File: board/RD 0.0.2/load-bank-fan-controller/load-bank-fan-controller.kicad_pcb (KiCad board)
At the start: 2 copper layers, 66.3 x 54.8 mm, 45 parts, among them J1 FAN1, J2 FAN2, J3 FAN3, J4 SPI, J5 UART, J6 12V IN, J7 TEMP1, J8 TEMP2, J9 RELAY, Q1 IRLML0030, Q2 IRLML0030, SW1 RESET, U1 AMS1117-5.0, U2 ATmega328P-A, U3 LM2904, Y1 Crystal

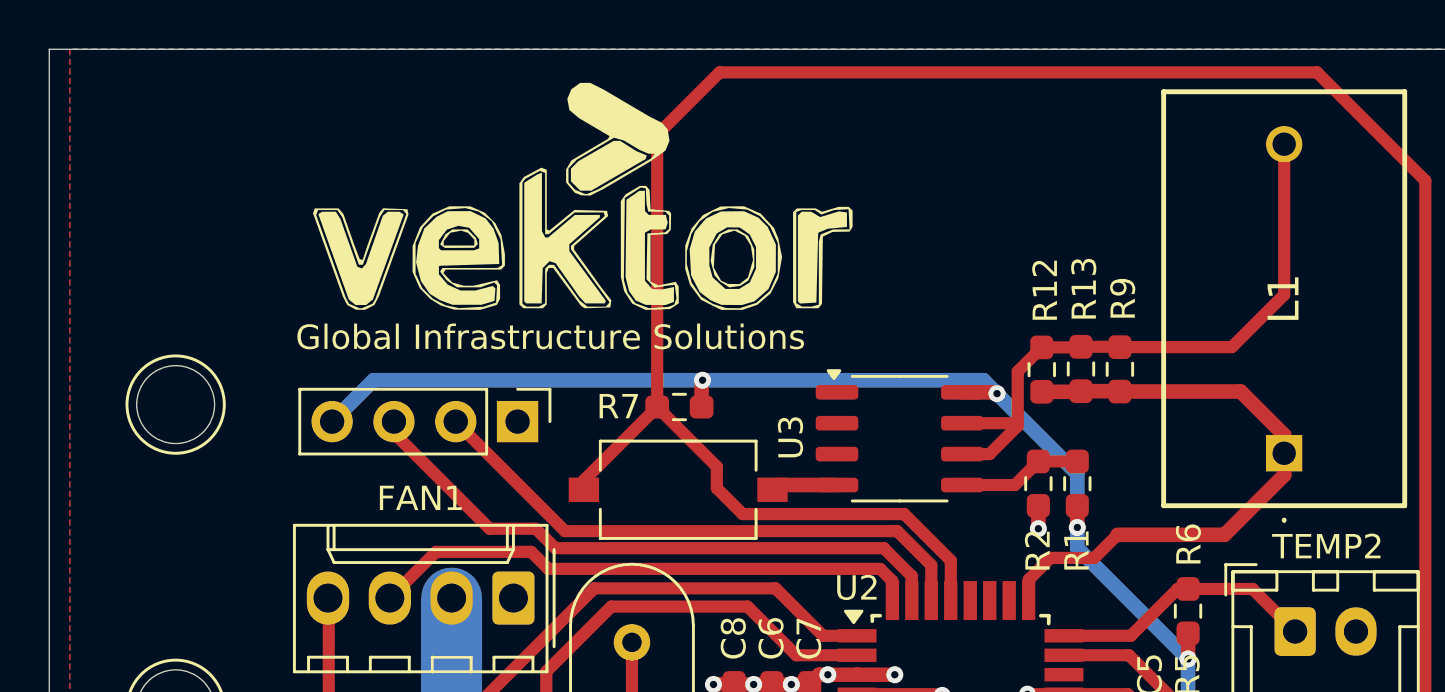
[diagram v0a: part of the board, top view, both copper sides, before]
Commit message: replace current sense resistor with the proper one
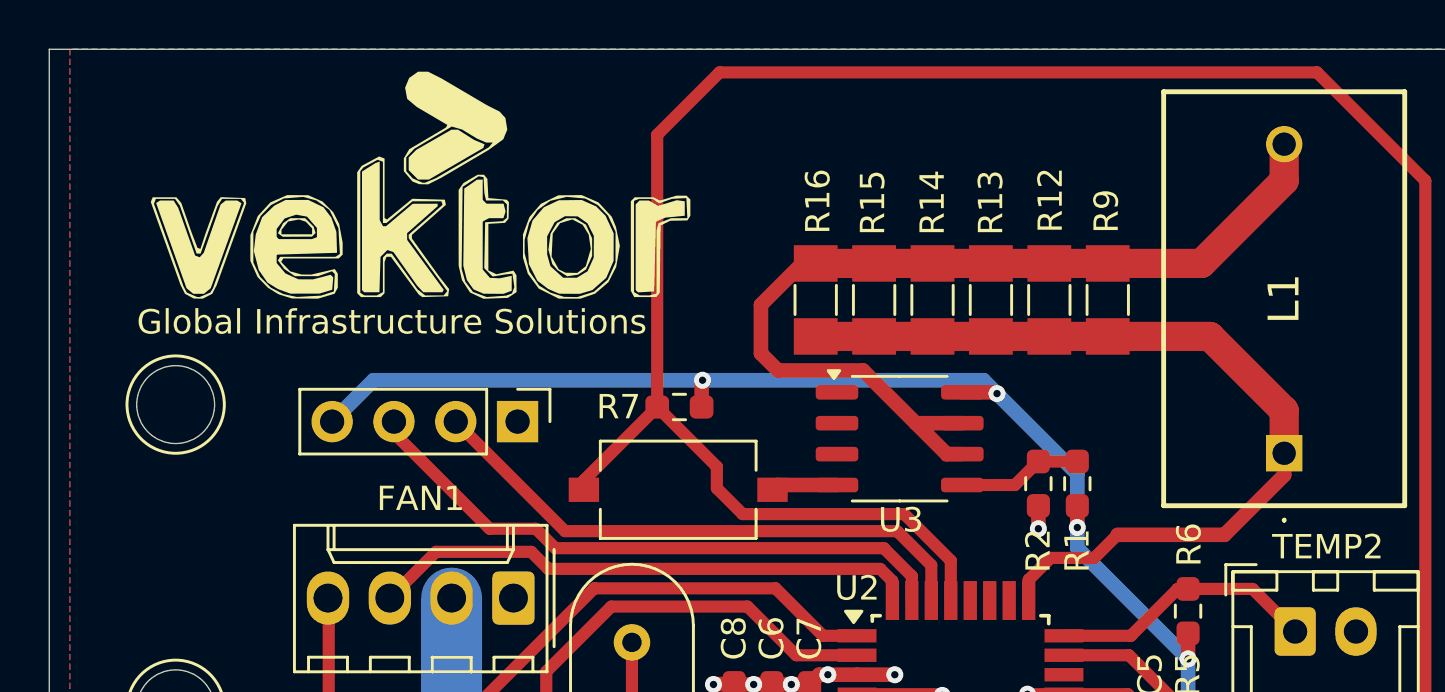
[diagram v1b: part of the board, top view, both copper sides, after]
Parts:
- added R14: 50R, Resistor_SMD:R_MiniMELF_MMA-0204, F.Cu at (145.3, 85.7)
- added R15: 50R, Resistor_SMD:R_MiniMELF_MMA-0204, F.Cu at (142.9, 85.7)
- added R16: 50R, Resistor_SMD:R_MiniMELF_MMA-0204, F.Cu at (140.6, 85.7)
- R12, R13, R9: value 25R -> 50R; footprint Resistor_SMD:R_0603_1608Metric_Pad0.98x0.95mm_HandSolder -> Resistor_SMD:R_MiniMELF_MMA-0204
- moved R13 4.66 mm to (147.8, 85.7)
- moved R9 2.89 mm to (152.6, 85.7)
- moved R12 2.88 mm to (150.2, 85.7)
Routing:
- net Net-(U3B--): track 25.8 -> 39.0 mm
- net CT: track 25.5 -> 36.3 mm

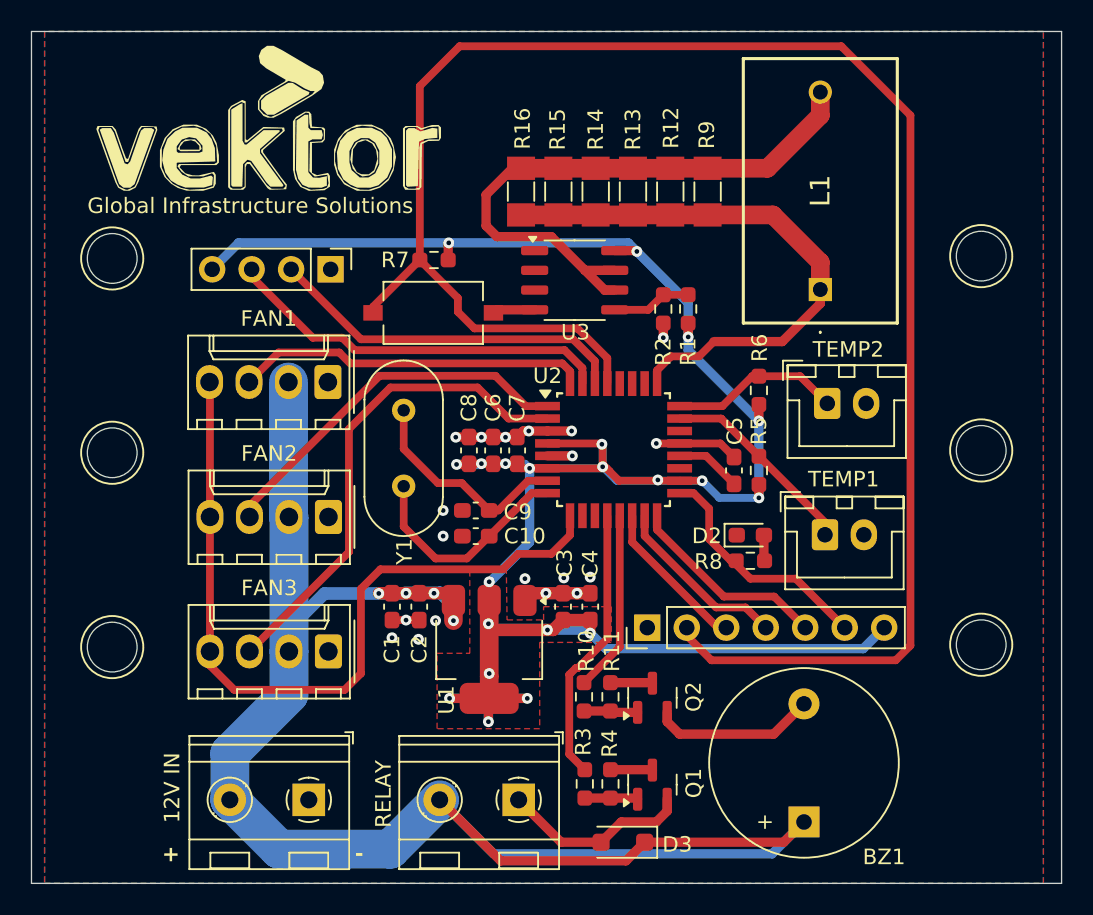
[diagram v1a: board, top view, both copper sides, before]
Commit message: connector changed and component added
change 12v connector, change spi to icsp connector, change  regulator input cap to 100u, remove uart conn, add diode to regulator input
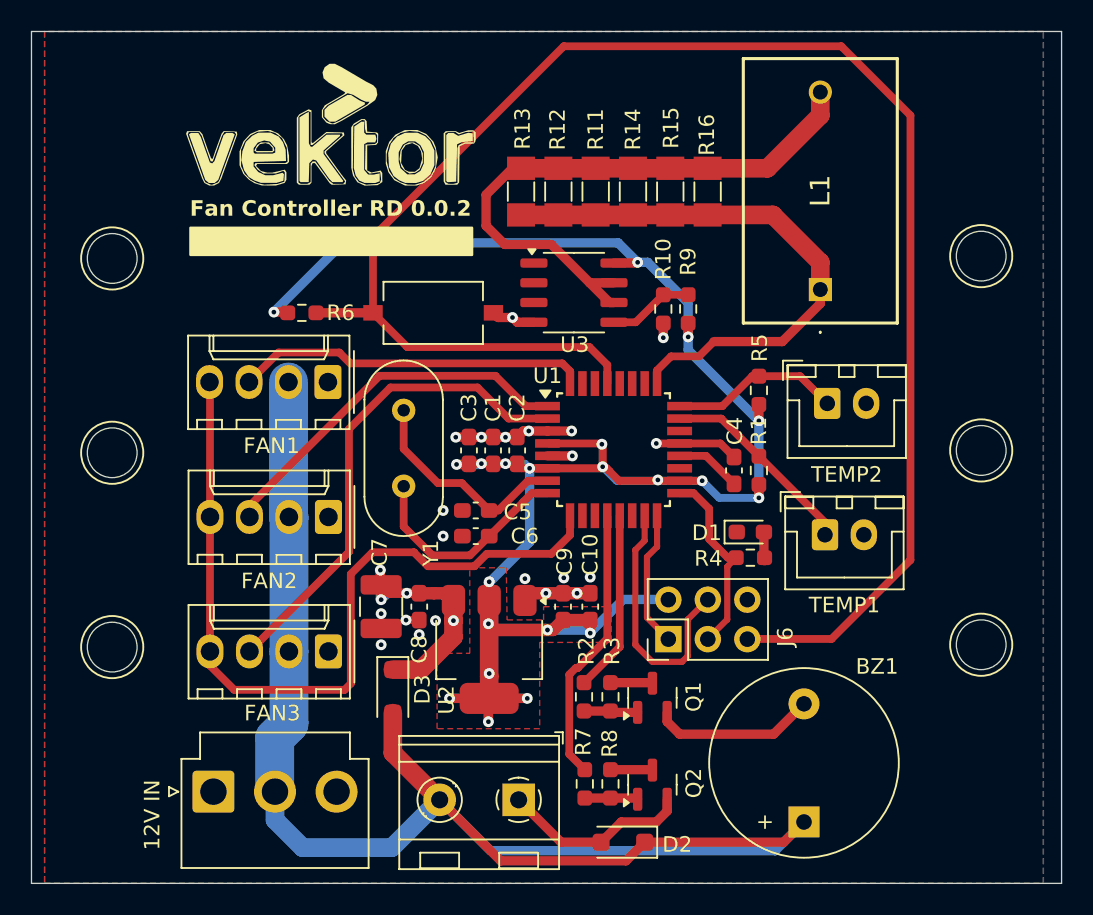
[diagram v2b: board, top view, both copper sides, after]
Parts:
- removed the J4 at (148.7, 113.7)
- removed the J5 at (128.3, 90.7)
- added D3: 1N4007, Diode_SMD:D_SOD-123F, F.Cu at (132.3, 117.8)
- added J8: 12V IN, Connector_JST:JST_VH_B3P-VH-B_1x03_P3.96mm_Vertical, F.Cu at (120.8, 124.2)
- C7: renamed from C1; value 1uF -> 100uF; footprint Capacitor_SMD:C_0603_1608Metric_Pad1.08x0.95mm_HandSolder -> Inductor_SMD:L_1210_3225Metric
- J6: value 12V IN -> ISP; footprint TerminalBlock_RND:TerminalBlock_RND_205-00232_1x02_P5.08mm_Horizontal -> Connector_PinHeader_2.54mm:PinHeader_2x03_P2.54mm_Vertical
- moved J6 25.3 mm to (150.0, 114.4), turned to 90 degrees
- moved R6 9.15 mm to (126.5, 93.5), turned to 0 degrees
- moved U3 0.80 mm to (143.9, 92.2)
- moved C7 0.70 mm to (131.6, 112.3)
- moved D1 0.20 mm to (155.3, 107.5)
- moved R4 0.20 mm to (155.3, 109.2)
- renumbered C6 to C1, C4 to C10, C7 to C2, C8 to C3, C5 to C4, C9 to C5, C10 to C6, C2 to C8, C3 to C9, D2 to D1, D3 to D2, DRA2 to DRA1, DRA1 to DRA2, J7 to J2, J9 to J3, J8 to J4, J2 to J5, J3 to J7, Q2 to Q1, Q1 to Q2, R5 to R1, R2 to R10, R14 to R11, R15 to R12, R16 to R13, R13 to R14, R12 to R15, R9 to R16, R10 to R2, R11 to R3, R8 to R4, R6 to R5, R7 to R6, R3 to R7, R4 to R8, R1 to R9, U2 to U1, U1 to U2
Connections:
- C7 pad 1: +12V -> +12VA
- C8 pad 1: +12V -> +12VA
- J6 pad 1: GND -> MISO
- J6 pad 2: +12V -> +5V
- U2 pad 3: +12V -> +12VA
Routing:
- net uC_TX: track 25.2 -> 0.00 mm
- net uC_RX: track 23.4 -> 0.00 mm
- net +12VA: track 0.00 -> 21.5 mm, vias 0 -> 4
- net +12V: track 121.2 -> 101.1 mm, vias 4 -> 0
- net +5V: track 168.7 -> 151.8 mm
- net SS: track 10.0 -> 0.00 mm
- net RESET: track 117.2 -> 108.9 mm
- net MOSI: track 11.5 -> 16.7 mm
- net MISO: track 13.0 -> 8.76 mm
- net SCK: track 15.5 -> 12.5 mm
- net FAN_PWM: track 50.6 -> 52.3 mm
- net GND: track 29.2 -> 28.7 mm, vias 19 -> 21
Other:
- board text removed: "+"
- board text removed: "-"
- board text removed: "Global Infrastructure Solutions"

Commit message: straighten the din rail mount
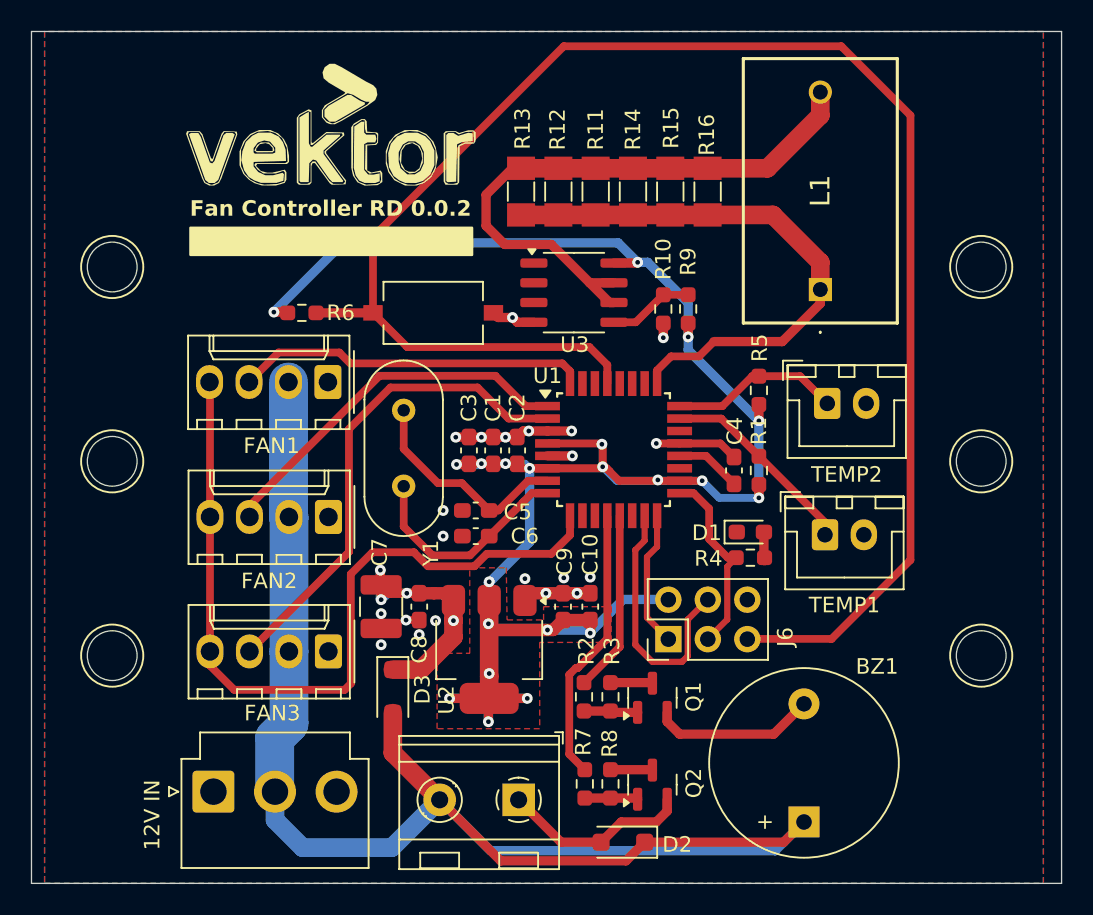
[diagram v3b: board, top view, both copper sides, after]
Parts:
- moved DRA1 0.70 mm to (170.2, 103.0)
- moved DRA2 0.55 mm to (114.2, 103.0)
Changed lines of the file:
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@@
 	(footprint "MountingEquipment:DINRailAdapter_3xM3_PhoenixContact_1201578"
 		(layer "F.Cu")
-		(at 170.15 102.3 90)
+		(at 170.15 103 90)
 		(descr "https://www.phoenixcontact.com/online/portal/us?uri=pxc-oc-itemdetail:pid=1201578&library=usen&tab=1")
 		(tags "DIN rail adapter universal three M3 clearance holes")
@@
 		)
 		(fp_text user "${REFERENCE}"
-			(at 1.27 2.54 360)
+			(at 1.27 2.54 0)
 			(layer "F.Fab")
 			(effects
@@
 		(tags "connector JST VH vertical")
 		(property "Reference" "J8"
-			(at 3.96 -4.9 360)
+			(at 3.96 -4.9 0)
 			(layer "F.SilkS")
 			(hide yes)
@@
 		)
 		(fp_text user "${REFERENCE}"
-			(at 3.96 4.1 360)
+			(at 3.96 4.1 0)
 			(layer "F.Fab")
 			(effects
@@
 		(tags "resistor handsolder")
 		(property "Reference" "R6"
-			(at 2.5 0 360)
+			(at 2.5 0 0)
 			(layer "F.SilkS")
 			(effects
@@
 		)
 		(property "Value" "1K"
-			(at 0 1.43 360)
+			(at 0 1.43 0)
 			(layer "F.Fab")
 			(effects
@@
 		)
 		(fp_text user "${REFERENCE}"
-			(at 0 0 360)
+			(at 0 0 0)
 			(layer "F.Fab")
 			(effects
@@
 		)
 		(property "Value" "RELAY"
-			(at 8.745 2.075 270)
+			(at 8.745 2.075 -90)
 			(layer "F.SilkS")
 			(hide yes)
@@
 		(fp_arc
 			(start -0.627362 -1.285823)
-			(mid -0.000201 -1.430703)
+			(mid -0.000201 -1.430702)
 			(end 0.627 -1.286)
 			(stroke
@@
 	(footprint "MountingEquipment:DINRailAdapter_3xM3_PhoenixContact_1201578"
 		(layer "F.Cu")
-		(at 114.25 102.45 90)
+		(at 114.25 103 90)
 		(descr "https://www.phoenixcontact.com/online/portal/us?uri=pxc-oc-itemdetail:pid=1201578&library=usen&tab=1")
 		(tags "DIN rail adapter universal three M3 clearance holes")

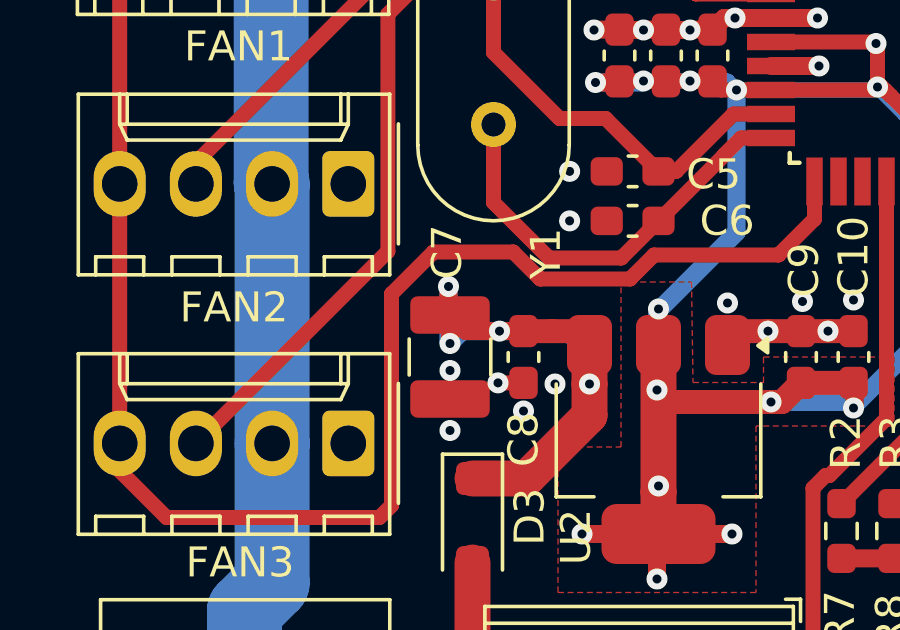
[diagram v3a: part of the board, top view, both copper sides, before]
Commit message: change wrong footprint from L_1210 to C_1210
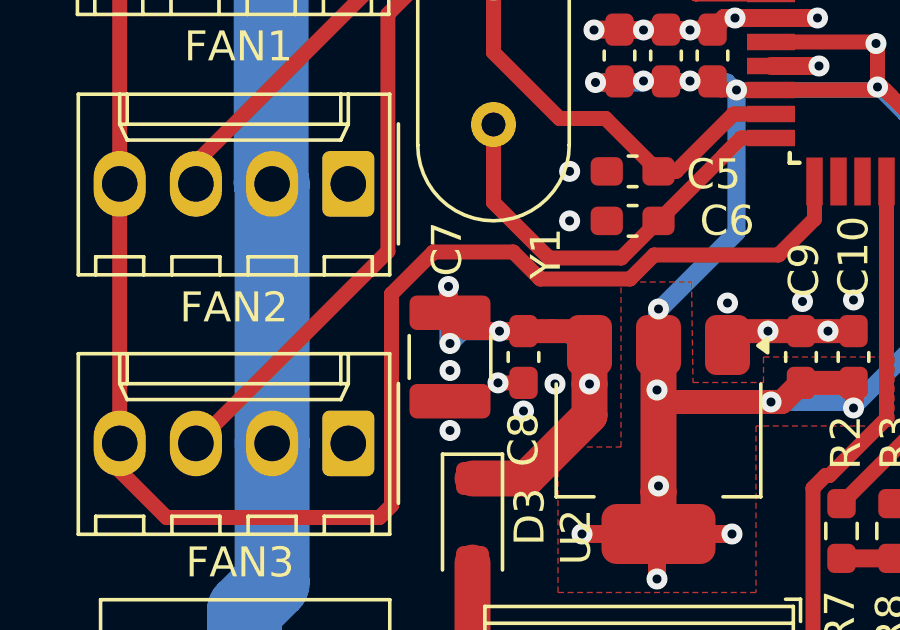
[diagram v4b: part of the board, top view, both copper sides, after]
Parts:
- C7: footprint Inductor_SMD:L_1210_3225Metric -> Capacitor_SMD:C_1210_3225Metric
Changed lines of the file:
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@@
 		)
 	)
-	(footprint "Inductor_SMD:L_1210_3225Metric"
+	(footprint "Capacitor_SMD:C_1210_3225Metric"
 		(layer "F.Cu")
 		(at 131.55 112.35 -90)
-		(descr "Inductor SMD 1210 (3225 Metric), square (rectangular) end terminal, IPC_7351 nominal, (Body size source: http://www.tortai-tech.com/upload/download/2011102023233369053.pdf), generated with kicad-footprint-generator")
-		(tags "inductor")
+		(descr "Capacitor SMD 1210 (3225 Metric), square (rectangular) end terminal, IPC_7351 nominal, (Body size source: IPC-SM-782 page 76, https://www.pcb-3d.com/wordpress/wp-content/uploads/ipc-sm-782a_amendment_1_and_2.pdf), generated with kicad-footprint-generator")
+		(tags "capacitor")
 		(property "Reference" "C7"
-			(at -3.5 0.1 -90)
+			(at -3.6 0.1 -90)
 			(layer "F.SilkS")
 			(effects
@@
 		)
 		(property "Value" "100uF"
-			(at 0 2.28 -90)
+			(at 0 2.3 -90)
 			(layer "F.Fab")
 			(effects
@@
 			)
 		)
-		(property "Footprint" "Inductor_SMD:L_1210_3225Metric"
+		(property "Footprint" "Capacitor_SMD:C_1210_3225Metric"
 			(at 0 0 -90)
 			(unlocked yes)
@@
 		(attr smd)
 		(fp_line
-			(start -0.602064 1.36)
-			(end 0.602064 1.36)
+			(start -0.711252 1.36)
+			(end 0.711252 1.36)
 			(stroke
 				(width 0.12)
@@
 		)
 		(fp_line
-			(start -0.602064 -1.36)
-			(end 0.602064 -1.36)
+			(start -0.711252 -1.36)
+			(end 0.711252 -1.36)
 			(stroke
 				(width 0.12)
@@
 		)
 		(fp_line
-			(start -2.28 1.58)
-			(end -2.28 -1.58)
+			(start -2.3 1.6)
+			(end -2.3 -1.6)
 			(stroke
 				(width 0.05)
@@
 		)
 		(fp_line
-			(start 2.28 1.58)
-			(end -2.28 1.58)
+			(start 2.3 1.6)
+			(end -2.3 1.6)
 			(stroke
 				(width 0.05)
@@
 		)
 		(fp_line
-			(start -2.28 -1.58)
-			(end 2.28 -1.58)
+			(start -2.3 -1.6)
+			(end 2.3 -1.6)
 			(stroke
 				(width 0.05)
@@
 		)
 		(fp_line
-			(start 2.28 -1.58)
-			(end 2.28 1.58)
+			(start 2.3 -1.6)
+			(end 2.3 1.6)
 			(stroke
 				(width 0.05)
@@
 		)
 		(pad "1" smd roundrect
-			(at -1.4 0 270)
-			(size 1.25 2.65)
+			(at -1.475 0 270)
+			(size 1.15 2.7)
 			(layers "F.Cu" "F.Paste" "F.Mask")
-			(roundrect_rratio 0.2)
+			(roundrect_rratio 0.217391)
 			(net 40 "+12VA")
 			(pintype "passive")
 		)
 		(pad "2" smd roundrect
-			(at 1.4 0 270)
-			(size 1.25 2.65)
+			(at 1.475 0 270)
+			(size 1.15 2.7)
 			(layers "F.Cu" "F.Paste" "F.Mask")
-			(roundrect_rratio 0.2)
+			(roundrect_rratio 0.217391)
 			(net 2 "GND")
 			(pintype "passive")
 		)
-		(model "${KICAD8_3DMODEL_DIR}/Inductor_SMD.3dshapes/L_1210_3225Metric.wrl"
+		(model "${KICAD8_3DMODEL_DIR}/Capacitor_SMD.3dshapes/C_1210_3225Metric.wrl"
 			(offset
 				(xyz 0 0 0)
@@
 		(fp_arc
 			(start -0.627362 -1.285823)
-			(mid -0.000201 -1.430702)
+			(mid -0.000201 -1.430701)
 			(end 0.627 -1.286)
 			(stroke
